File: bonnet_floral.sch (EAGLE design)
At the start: 10 parts, among them IC1 RASPBERRY_PI_ZERO_W_(V1.3)-WO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

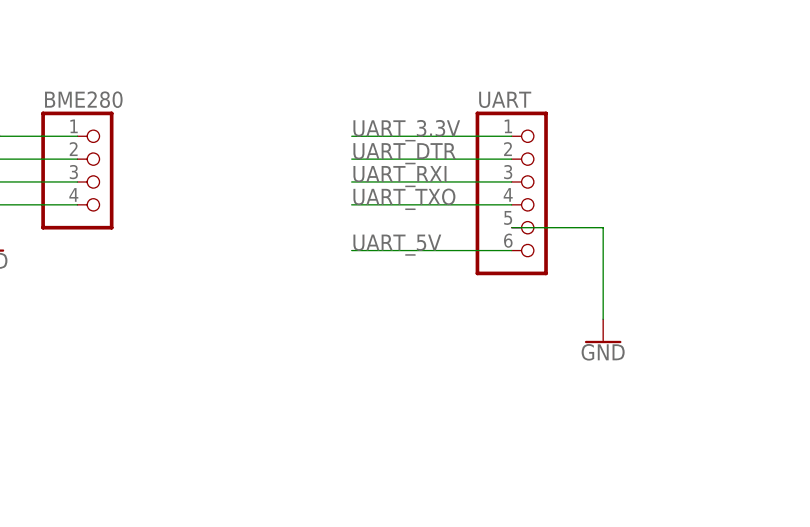
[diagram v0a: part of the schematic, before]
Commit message: Add Serial Port 5V power feed
So in the original design the power coming from the serial port header
was intentionally left N/C, however there's argument that this might
have made some learning applications more complicated / expensive.
Attaching it to the main PI header 5V looks like it should work, and
feed into the same 5V linke the normal power header does.  Since the 5V
coming from the serial port chip seems to also feed directly from the
USB port this should be, at least, as safe as running power to it via
the main power header.

Signed-off-by: John 'Warthog9' Hawley <warthog9@eaglescrag.net>
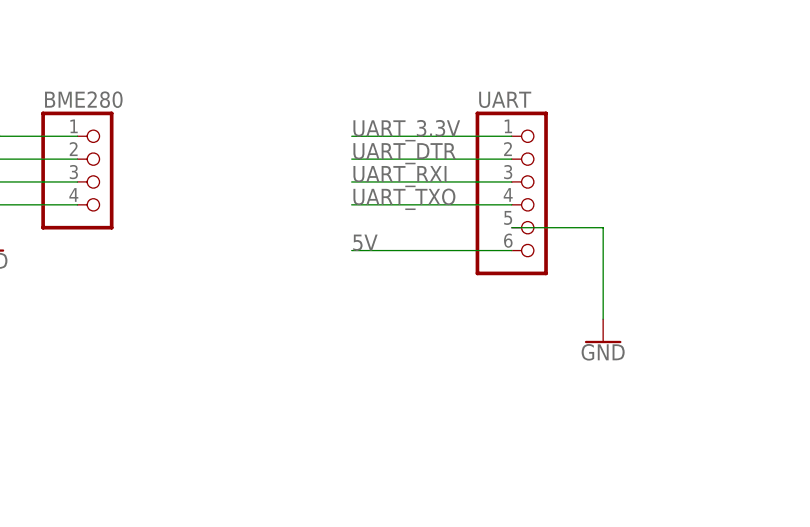
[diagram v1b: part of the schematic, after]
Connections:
- removed net UART_5V: UART.6
- net 5V: now also UART.6
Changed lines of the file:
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@@
 <wire x1="12.7" y1="73.66" x2="12.7" y2="81.28" width="0.1524" layer="91"/>
+</segment>
+<segment>
+<pinref part="UART" gate="A" pin="6"/>
+<wire x1="154.94" y1="218.44" x2="137.16" y2="218.44" width="0.1524" layer="91"/>
+<label x="137.16" y="218.44" size="1.778" layer="95"/>
 </segment>
 </net>
@@
 </segment>
 </net>
-<net name="UART_5V" class="0">
-<segment>
-<pinref part="UART" gate="A" pin="6"/>
-<wire x1="154.94" y1="218.44" x2="137.16" y2="218.44" width="0.1524" layer="91"/>
-<label x="137.16" y="218.44" size="1.778" layer="95"/>
-</segment>
-</net>
